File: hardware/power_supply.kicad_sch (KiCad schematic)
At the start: 0 parts

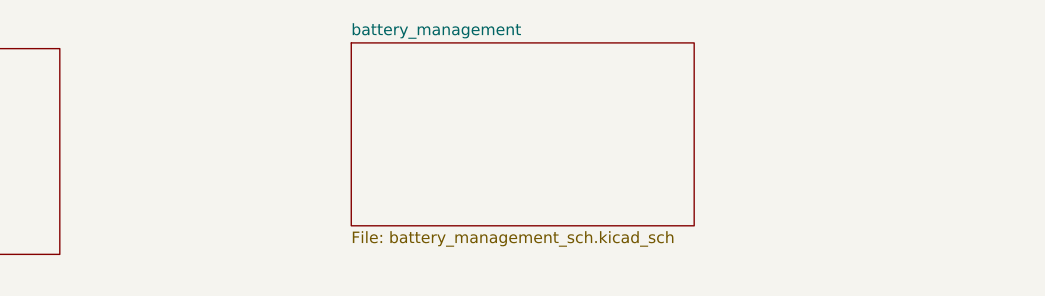
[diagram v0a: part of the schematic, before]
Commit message: Rought draft of battery charger and started SEPIC stage
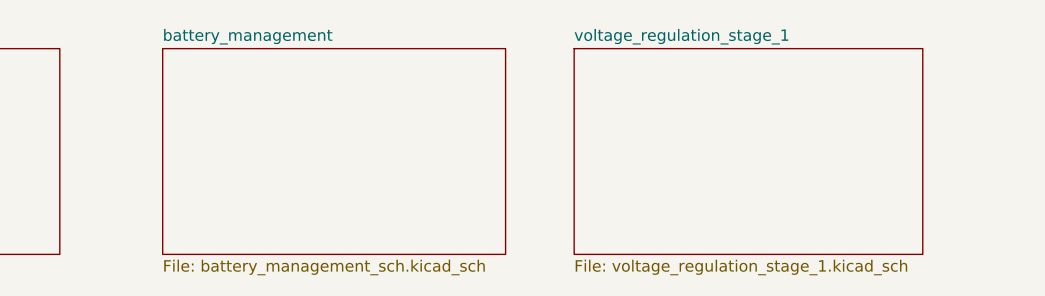
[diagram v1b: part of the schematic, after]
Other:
- added sheet voltage_regulation_stage_1 (voltage_regulation_stage_1.kicad_sch)
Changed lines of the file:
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@@
     )
   )
-  (sheet (at 106.045 28.575) (size 38.1 20.32) (fields_autoplaced)
+  (sheet (at 85.09 29.21) (size 38.1 22.86) (fields_autoplaced)
     (stroke (width 0.1524) (type solid))
     (fill (color 0 0 0 0.0000))
-    (property "Sheetname" "battery_management" (at 106.045 27.8634 0)
+    (property "Sheetname" "battery_management" (at 85.09 28.4984 0)
       (effects (font (size 1.27 1.27)) (justify left bottom))
     )
-    (property "Sheetfile" "battery_management_sch.kicad_sch" (at 106.045 49.4796 0)
+    (property "Sheetfile" "battery_management_sch.kicad_sch" (at 85.09 52.6546 0)
       (effects (font (size 1.27 1.27)) (justify left top))
     )
@@
       )
     )
+  )
+  (sheet (at 130.81 29.21) (size 38.735 22.86) (fields_autoplaced)
+    (stroke (width 0.1524) (type solid))
+    (fill (color 0 0 0 0.0000))
+    (property "Sheetname" "voltage_regulation_stage_1" (at 130.81 28.4984 0)
+      (effects (font (size 1.27 1.27)) (justify left bottom))
+    )
+    (property "Sheetfile" "voltage_regulation_stage_1.kicad_sch" (at 130.81 52.6546 0)
+      (effects (font (size 1.27 1.27)) (justify left top))
+    )
+    (instances
+      (project "power_supply"
+        (path "/3169906c-dcce-4761-b072-54530f8b9e50" (page "4"))
+      )
+    )

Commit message: Continued work on schematic.
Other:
- added sheet voltage_regualtion_stage_2 (voltage_regualtion_stage_2.kicad_sch)
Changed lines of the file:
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@@
 (kicad_sch (version 20230121) (generator eeschema)
   (paper "A4")
+  (sheet (at 178.435 29.21) (size 39.37 22.86) (fields_autoplaced)
+    (stroke (width 0.1524) (type solid))
+    (fill (color 0 0 0 0.0000))
+    (property "Sheetname" "voltage_regualtion_stage_2" (at 178.435 28.4984 0)
+      (effects (font (size 1.27 1.27)) (justify left bottom))
+    )
+    (property "Sheetfile" "voltage_regualtion_stage_2.kicad_sch" (at 178.435 52.6546 0)
+      (effects (font (size 1.27 1.27)) (justify left top))
+    )
+    (instances
+      (project "power_supply"
+        (path "/3169906c-dcce-4761-b072-54530f8b9e50" (page "5"))
+      )
+    )
+  )
   (sheet (at 30.48 29.21) (size 43.18 22.86) (fields_autoplaced)
     (stroke (width 0.1524) (type solid))

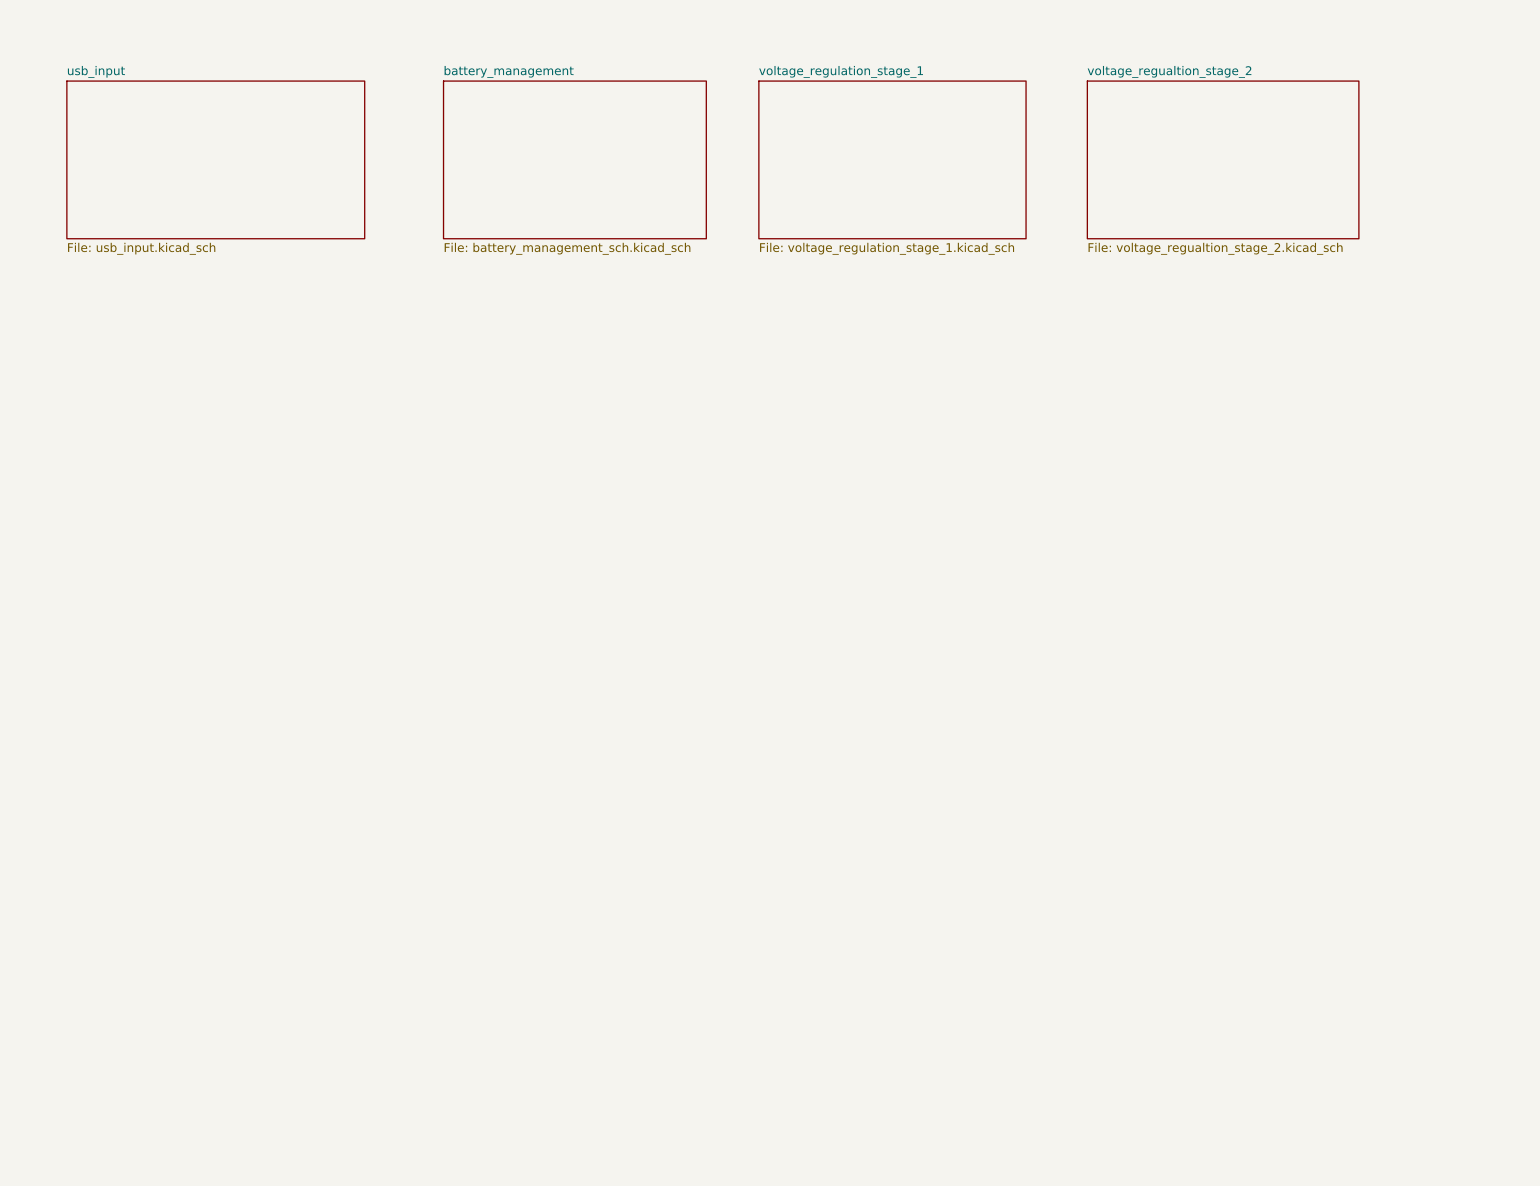
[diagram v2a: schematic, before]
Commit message: Component values chosen for bat. charge, bat. protect, USB input
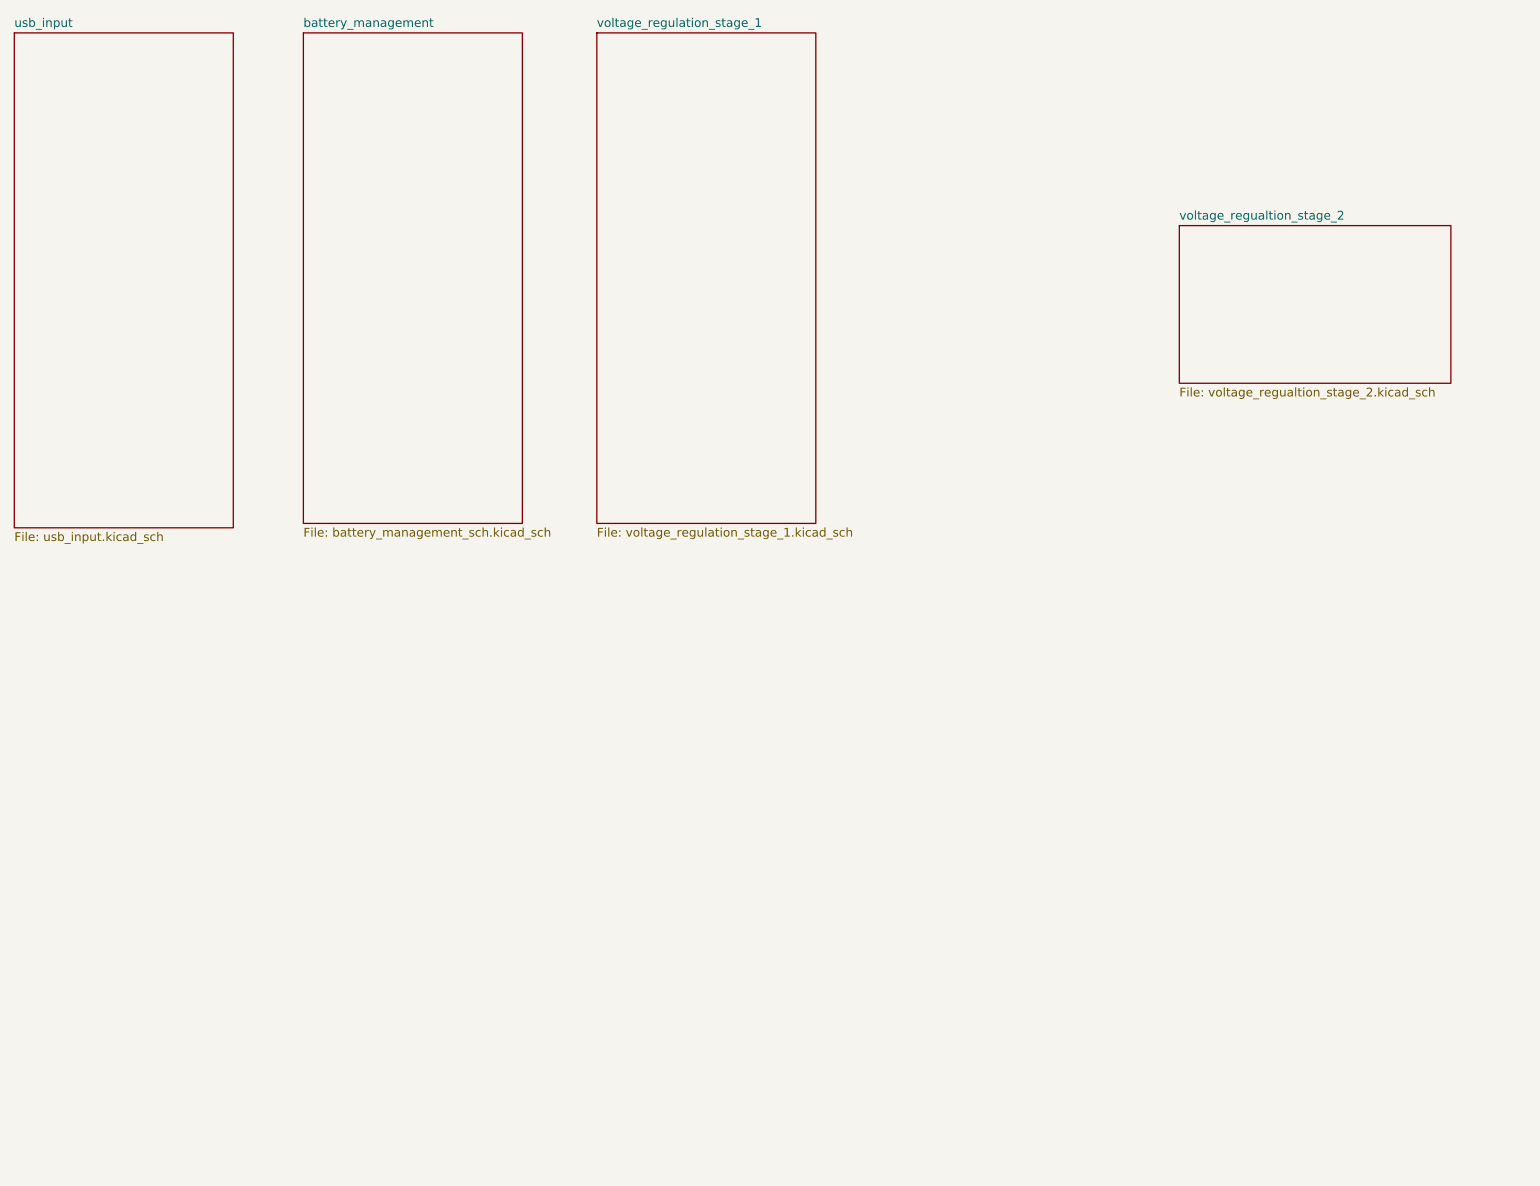
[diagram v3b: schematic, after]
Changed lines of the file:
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@@
 (kicad_sch (version 20230121) (generator eeschema)
-  (paper "A4")
-  (sheet (at 178.435 29.21) (size 39.37 22.86) (fields_autoplaced)
+  (paper "USLetter")
+  (sheet (at 191.77 50.165) (size 39.37 22.86) (fields_autoplaced)
     (stroke (width 0.1524) (type solid))
     (fill (color 0 0 0 0.0000))
-    (property "Sheetname" "voltage_regualtion_stage_2" (at 178.435 28.4984 0)
+    (property "Sheetname" "voltage_regualtion_stage_2" (at 191.77 49.4534 0)
       (effects (font (size 1.27 1.27)) (justify left bottom))
     )
-    (property "Sheetfile" "voltage_regualtion_stage_2.kicad_sch" (at 178.435 52.6546 0)
+    (property "Sheetfile" "voltage_regualtion_stage_2.kicad_sch" (at 191.77 73.6096 0)
       (effects (font (size 1.27 1.27)) (justify left top))
     )
@@
     )
   )
-  (sheet (at 30.48 29.21) (size 43.18 22.86) (fields_autoplaced)
+  (sheet (at 22.86 22.225) (size 31.75 71.755) (fields_autoplaced)
     (stroke (width 0.1524) (type solid))
     (fill (color 0 0 0 0.0000))
-    (property "Sheetname" "usb_input" (at 30.48 28.4984 0)
+    (property "Sheetname" "usb_input" (at 22.86 21.5134 0)
       (effects (font (size 1.27 1.27)) (justify left bottom))
     )
-    (property "Sheetfile" "usb_input.kicad_sch" (at 30.48 52.6546 0)
+    (property "Sheetfile" "usb_input.kicad_sch" (at 22.86 94.5646 0)
       (effects (font (size 1.27 1.27)) (justify left top))
     )
@@
     )
   )
-  (sheet (at 85.09 29.21) (size 38.1 22.86) (fields_autoplaced)
+  (sheet (at 64.77 22.225) (size 31.75 71.12) (fields_autoplaced)
     (stroke (width 0.1524) (type solid))
     (fill (color 0 0 0 0.0000))
-    (property "Sheetname" "battery_management" (at 85.09 28.4984 0)
+    (property "Sheetname" "battery_management" (at 64.77 21.5134 0)
       (effects (font (size 1.27 1.27)) (justify left bottom))
     )
-    (property "Sheetfile" "battery_management_sch.kicad_sch" (at 85.09 52.6546 0)
+    (property "Sheetfile" "battery_management_sch.kicad_sch" (at 64.77 93.9296 0)
       (effects (font (size 1.27 1.27)) (justify left top))
     )
@@
     )
   )
-  (sheet (at 130.81 29.21) (size 38.735 22.86) (fields_autoplaced)
+  (sheet (at 107.315 22.225) (size 31.75 71.12) (fields_autoplaced)
     (stroke (width 0.1524) (type solid))
     (fill (color 0 0 0 0.0000))
-    (property "Sheetname" "voltage_regulation_stage_1" (at 130.81 28.4984 0)
+    (property "Sheetname" "voltage_regulation_stage_1" (at 107.315 21.5134 0)
       (effects (font (size 1.27 1.27)) (justify left bottom))
     )
-    (property "Sheetfile" "voltage_regulation_stage_1.kicad_sch" (at 130.81 52.6546 0)
+    (property "Sheetfile" "voltage_regulation_stage_1.kicad_sch" (at 107.315 93.9296 0)
       (effects (font (size 1.27 1.27)) (justify left top))
     )

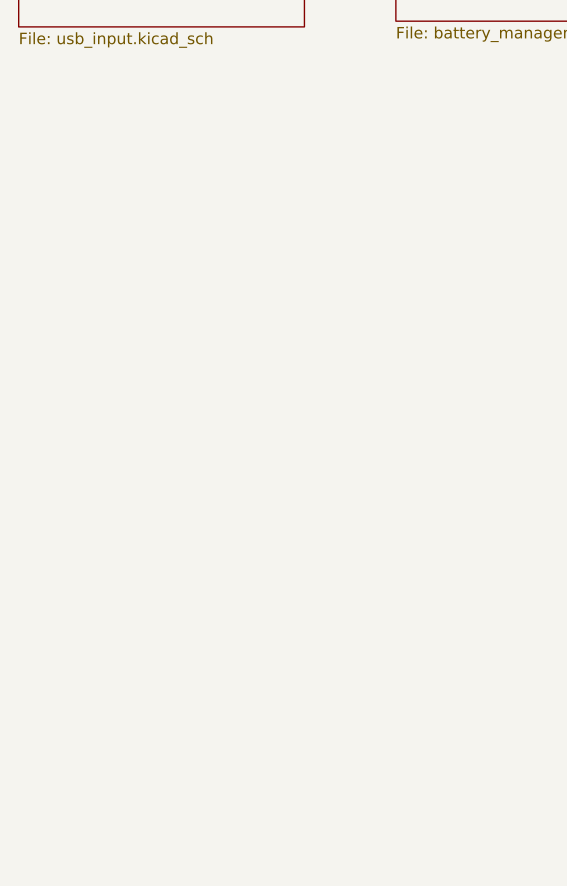
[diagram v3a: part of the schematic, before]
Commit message: Most work finished on stage1. Moving on to stage2.
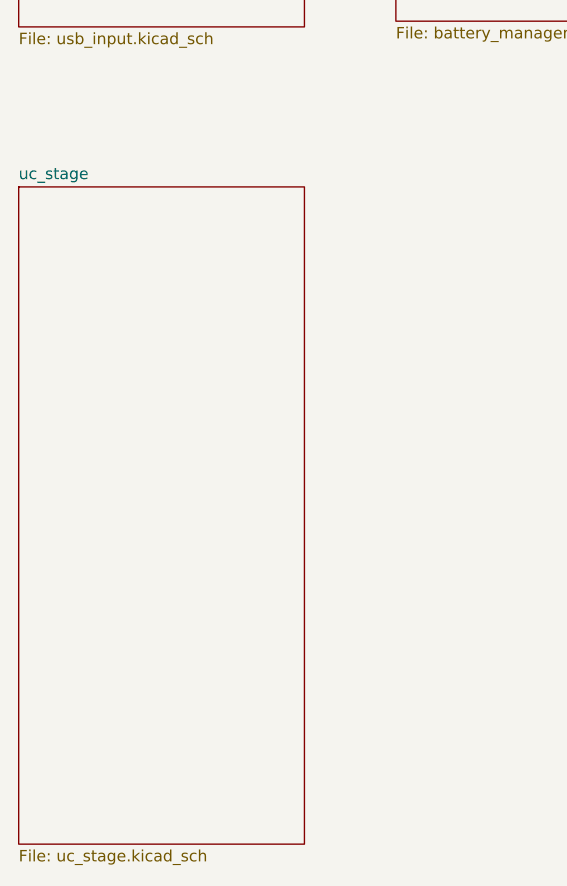
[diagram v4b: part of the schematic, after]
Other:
- added sheet uc_stage (uc_stage.kicad_sch)
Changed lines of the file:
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@@
+    )
+  )
+  (sheet (at 22.86 111.76) (size 31.75 73.025) (fields_autoplaced)
+    (stroke (width 0.1524) (type solid))
+    (fill (color 0 0 0 0.0000))
+    (property "Sheetname" "uc_stage" (at 22.86 111.0484 0)
+      (effects (font (size 1.27 1.27)) (justify left bottom))
+    )
+    (property "Sheetfile" "uc_stage.kicad_sch" (at 22.86 185.3696 0)
+      (effects (font (size 1.27 1.27)) (justify left top))
+    )
+    (instances
+      (project "power_supply"
+        (path "/3169906c-dcce-4761-b072-54530f8b9e50" (page "6"))
+      )
     )
   )

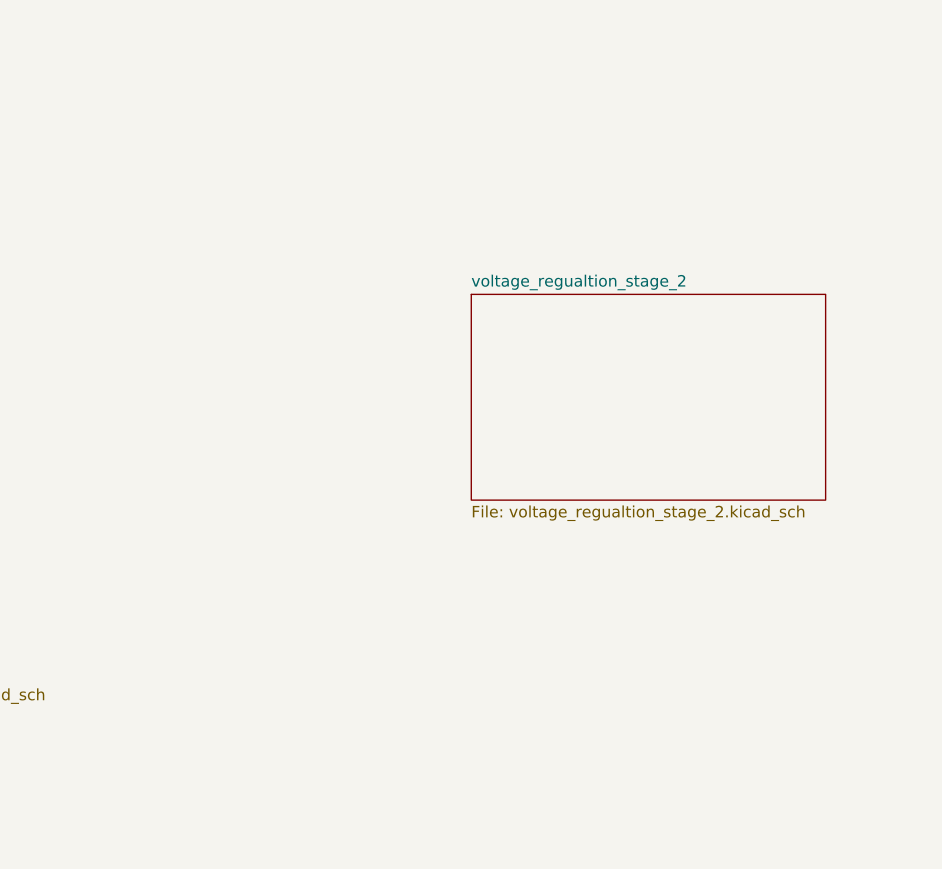
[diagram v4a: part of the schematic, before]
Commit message: More simulation and work done on SEPIC stage. MOSFET changes to USB stage and charging stage.
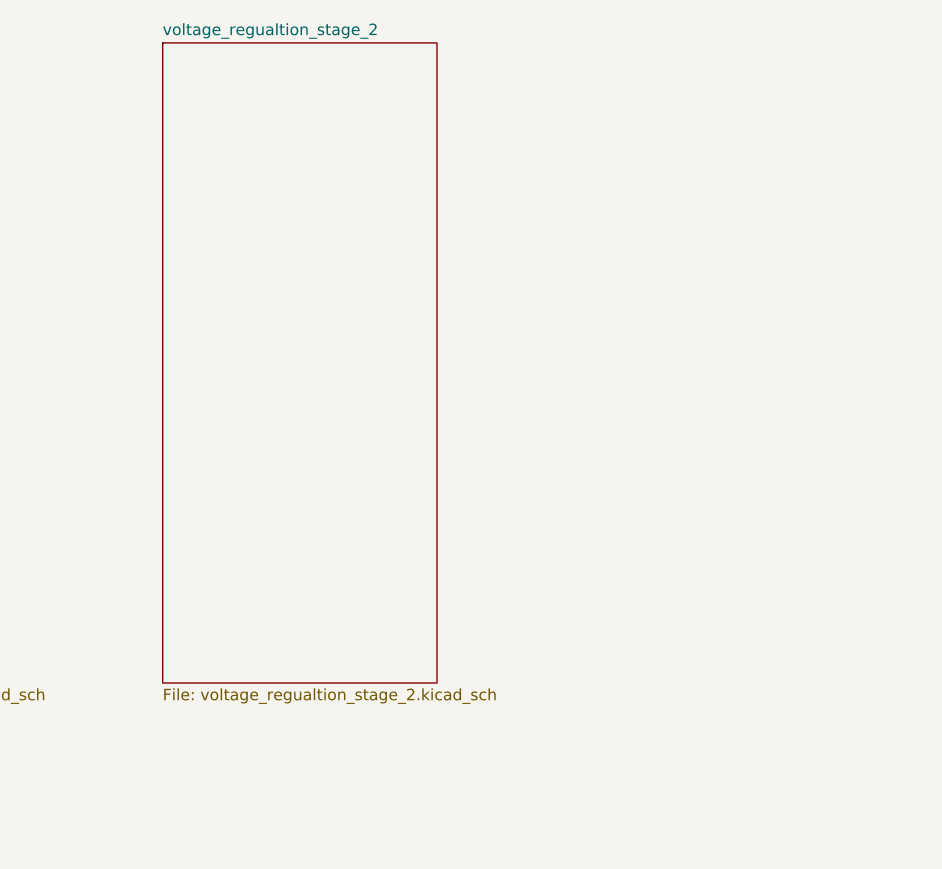
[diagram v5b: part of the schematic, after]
